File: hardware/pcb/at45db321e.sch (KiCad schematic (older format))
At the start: 2 parts

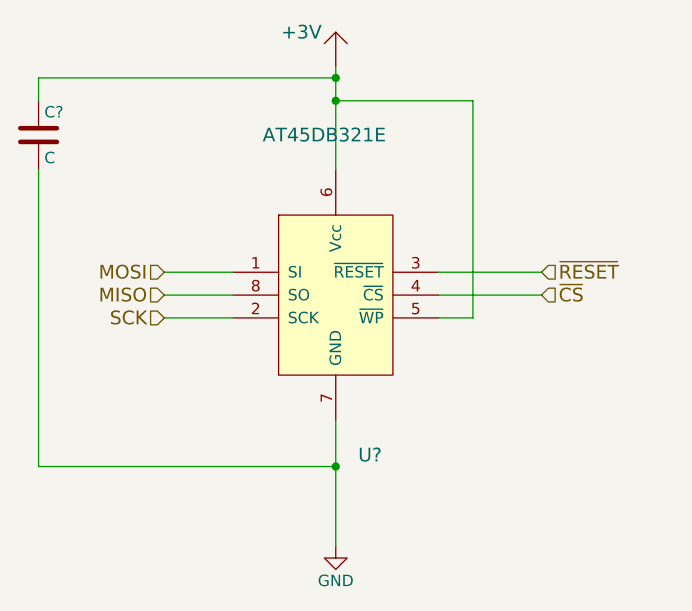
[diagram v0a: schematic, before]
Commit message: Added component values
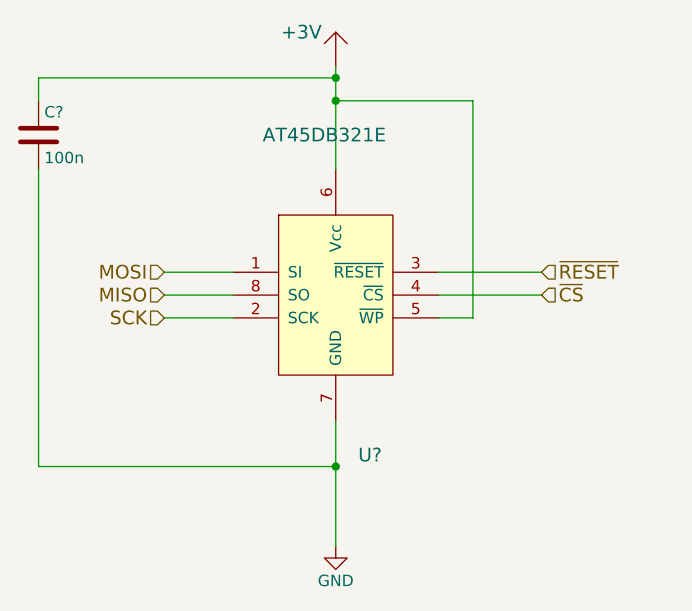
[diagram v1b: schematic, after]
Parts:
- C?: value C -> 100n
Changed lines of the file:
@@
 P 4150 3050
 F 0 "C?" H 4175 3150 50  0000 L CNN
-F 1 "C" H 4175 2950 50  0000 L CNN
+F 1 "100n" H 4175 2950 50  0000 L CNN
 F 2 "" H 4188 2900 30  0000 C CNN
 F 3 "" H 4150 3050 60  0000 C CNN

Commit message: more changes
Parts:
- C25: renamed from C?; value 100n -> 100nF
- gave numbers to parts that had none: 1
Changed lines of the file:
@@
 $EndDescr
 $Comp
-L AT45DB321E U?
+L AT45DB321E U7
 U 1 1 552F3DBF
 P 5450 3700
-F 0 "U?" H 5600 2950 60  0000 C CNN
+F 0 "U7" H 5600 2950 60  0000 C CNN
 F 1 "AT45DB321E" H 5400 4350 60  0000 C CNN
 F 2 "" H 5500 3350 60  0000 C CNN
@@
 $EndComp
 $Comp
-L +3V #PWR033
+L +3V #PWR40
 U 1 1 552F3DDF
 P 5450 2750
-F 0 "#PWR033" H 5450 2650 60  0001 C CNN
+F 0 "#PWR40" H 5450 2650 60  0001 C CNN
 F 1 "+3V" H 5300 2900 60  0000 C CNN
 F 2 "" H 5450 2750 60  0000 C CNN
@@
 	5450 3200 5450 2750
 $Comp
-L GND #PWR034
+L GND #PWR41
 U 1 1 552F3DF8
 P 5450 4850
-F 0 "#PWR034" H 5450 4600 50  0001 C CNN
+F 0 "#PWR41" H 5450 4600 50  0001 C CNN
 F 1 "GND" H 5450 4700 50  0000 C CNN
 F 2 "" H 5450 4850 60  0000 C CNN
@@
 	6350 3650 5900 3650
 $Comp
-L C C?
+L C C25
 U 1 1 552F40C6
 P 4150 3050
-F 0 "C?" H 4175 3150 50  0000 L CNN
-F 1 "100n" H 4175 2950 50  0000 L CNN
+F 0 "C25" H 4175 3150 50  0000 L CNN
+F 1 "100nF" H 4175 2950 50  0000 L CNN
 F 2 "" H 4188 2900 30  0000 C CNN
 F 3 "" H 4150 3050 60  0000 C CNN

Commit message: mega commit
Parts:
- C27: renamed from C25; footprint (none) -> Capacitors_SMD:C_0603
- U5: renamed from U7; footprint (none) -> aero:UDFN-8
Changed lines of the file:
@@
 $EndDescr
 $Comp
-L AT45DB321E U7
+L AT45DB321E U5
 U 1 1 552F3DBF
 P 5450 3700
-F 0 "U7" H 5600 2950 60  0000 C CNN
+F 0 "U5" H 5600 2950 60  0000 C CNN
 F 1 "AT45DB321E" H 5400 4350 60  0000 C CNN
-F 2 "" H 5500 3350 60  0000 C CNN
+F 2 "aero:UDFN-8" H 5500 3350 60  0001 C CNN
 F 3 "" H 5500 3350 60  0000 C CNN
 	1    5450 3700
@@
 $EndComp
 $Comp
-L +3V #PWR40
+L +3V #PWR041
 U 1 1 552F3DDF
 P 5450 2750
-F 0 "#PWR40" H 5450 2650 60  0001 C CNN
+F 0 "#PWR041" H 5450 2650 60  0001 C CNN
 F 1 "+3V" H 5300 2900 60  0000 C CNN
 F 2 "" H 5450 2750 60  0000 C CNN
@@
 	5450 3200 5450 2750
 $Comp
-L GND #PWR41
+L GND #PWR042
 U 1 1 552F3DF8
 P 5450 4850
-F 0 "#PWR41" H 5450 4600 50  0001 C CNN
+F 0 "#PWR042" H 5450 4600 50  0001 C CNN
 F 1 "GND" H 5450 4700 50  0000 C CNN
 F 2 "" H 5450 4850 60  0000 C CNN
@@
 	6350 3650 5900 3650
 $Comp
-L C C25
+L C C27
 U 1 1 552F40C6
 P 4150 3050
-F 0 "C25" H 4175 3150 50  0000 L CNN
+F 0 "C27" H 4175 3150 50  0000 L CNN
 F 1 "100nF" H 4175 2950 50  0000 L CNN
-F 2 "" H 4188 2900 30  0000 C CNN
+F 2 "Capacitors_SMD:C_0603" H 4188 2900 30  0001 C CNN
 F 3 "" H 4150 3050 60  0000 C CNN
 	1    4150 3050

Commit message: pre major restructuring commit
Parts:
- C24: renamed from C27; footprint Capacitors_SMD:C_0603 -> Capacitors_SMD:C_0402
- renumbered U5 to U6
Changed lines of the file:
@@
 $Descr A4 11693 8268
 encoding utf-8
-Sheet 5 7
+Sheet 5 8
 Title ""
 Date ""
@@
 $EndDescr
 $Comp
-L AT45DB321E U5
+L AT45DB321E U6
 U 1 1 552F3DBF
 P 5450 3700
-F 0 "U5" H 5600 2950 60  0000 C CNN
+F 0 "U6" H 5600 2950 60  0000 C CNN
 F 1 "AT45DB321E" H 5400 4350 60  0000 C CNN
 F 2 "aero:UDFN-8" H 5500 3350 60  0001 C CNN
@@
 $EndComp
 $Comp
-L +3V #PWR041
+L +3V #PWR037
 U 1 1 552F3DDF
 P 5450 2750
-F 0 "#PWR041" H 5450 2650 60  0001 C CNN
+F 0 "#PWR037" H 5450 2650 60  0001 C CNN
 F 1 "+3V" H 5300 2900 60  0000 C CNN
 F 2 "" H 5450 2750 60  0000 C CNN
@@
 	5450 3200 5450 2750
 $Comp
-L GND #PWR042
+L GND #PWR038
 U 1 1 552F3DF8
 P 5450 4850
-F 0 "#PWR042" H 5450 4600 50  0001 C CNN
+F 0 "#PWR038" H 5450 4600 50  0001 C CNN
 F 1 "GND" H 5450 4700 50  0000 C CNN
 F 2 "" H 5450 4850 60  0000 C CNN
@@
 	6350 3650 5900 3650
 $Comp
-L C C27
+L C C24
 U 1 1 552F40C6
 P 4150 3050
-F 0 "C27" H 4175 3150 50  0000 L CNN
+F 0 "C24" H 4175 3150 50  0000 L CNN
 F 1 "100nF" H 4175 2950 50  0000 L CNN
-F 2 "Capacitors_SMD:C_0603" H 4188 2900 30  0001 C CNN
+F 2 "Capacitors_SMD:C_0402" H 4188 2900 30  0001 C CNN
 F 3 "" H 4150 3050 60  0000 C CNN
 	1    4150 3050

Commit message: more progress on new layout
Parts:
- renumbered C24 to C22
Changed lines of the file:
@@
 	6350 3650 5900 3650
 $Comp
-L C C24
+L C C22
 U 1 1 552F40C6
 P 4150 3050
-F 0 "C24" H 4175 3150 50  0000 L CNN
+F 0 "C22" H 4175 3150 50  0000 L CNN
 F 1 "100nF" H 4175 2950 50  0000 L CNN
 F 2 "Capacitors_SMD:C_0402" H 4188 2900 30  0001 C CNN
